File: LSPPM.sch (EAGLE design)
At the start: 340 parts, among them IC1 ATMEGA328P QFN32, IC10 ATMEGA328P QFN32, IC11 ATMEGA328P QFN32, IC12 ATMEGA328P QFN32, IC13 ATMEGA328P QFN32, IC14 ATMEGA328P QFN32, IC15 ATMEGA328P QFN32, IC16 ATMEGA328P QFN32, IC17 TXB0104, IC18 TMP102, IC19 TMP102, IC2 ATMEGA328P QFN32, IC20 ATMEGA2561-16MU, IC21 MAX4372F, IC22 MAX4372F, IC23 MUX-74HC4067-QFNSMT, IC24 MUX-74HC4067-QFNSMT, IC25 TCA9555QFN, IC3 ATMEGA328P QFN32, IC4 ATMEGA328P QFN32, IC5 ATMEGA328P QFN32, IC6 ATMEGA328P QFN32, IC7 ATMEGA328P QFN32, IC8 ATMEGA328P QFN32, IC9 ATMEGA328P QFN32, P1 microSD, Q1 RJU003N03 N-MOSFET, Q10 RJU003N03 N-MOSFET, Q11 RJU003N03 N-MOSFET, Q12 RJU003N03 N-MOSFET, Q13 RJU003N03 N-MOSFET, Q14 RJU003N03 N-MOSFET, Q15 RJU003N03 N-MOSFET, Q16 RJU003N03 N-MOSFET, Q17 RJU003N03 N-MOSFET, Q18 RJU003N03 N-MOSFET, Q19 RJU003N03 N-MOSFET, Q2 RJU003N03 N-MOSFET, Q20 RJU003N03 N-MOSFET, Q21 RJU003N03 N-MOSFET, Q22 RJU003N03 N-MOSFET, Q23 RJU003N03 N-MOSFET, Q24 RJU003N03 N-MOSFET, Q25 RJU003N03 N-MOSFET, Q26 RJU003N03 N-MOSFET, Q27 RJU003N03 N-MOSFET, Q28 RJU003N03 N-MOSFET, Q29 RJU003N03 N-MOSFET, Q3 RJU003N03 N-MOSFET, Q30 RJU003N03 N-MOSFET, Q31 RJU003N03 N-MOSFET, Q32 RJU003N03 N-MOSFET, Q33 RJU003N03 N-MOSFET, Q34 RJU003N03 N-MOSFET, Q35 RJU003N03 N-MOSFET, Q36 RJU003N03 N-MOSFET, Q37 RJU003N03 N-MOSFET, Q38 RJU003N03 N-MOSFET, Q39 RJU003N03 N-MOSFET, Q4 RJU003N03 N-MOSFET, Q40 RJU003N03 N-MOSFET, Q41 RJU003N03 N-MOSFET, Q42 RJU003N03 N-MOSFET, Q43 RJU003N03 N-MOSFET, Q44 RJU003N03 N-MOSFET, Q45 RJU003N03 N-MOSFET, Q46 RJU003N03 N-MOSFET, Q5 RJU003N03 N-MOSFET, Q6 RJU003N03 N-MOSFET, Q7 RJU003N03 N-MOSFET, Q8 RJU003N03 N-MOSFET, Q9 RJU003N03 N-MOSFET, SW1 ADG801 SOT23-6, SW10 ADG801 SOT23-6, SW11 ADG801 SOT23-6, SW12 ADG801 SOT23-6, SW13 ADG801 SOT23-6, SW14 ADG801 SOT23-6, SW15 ADG801 SOT23-6, SW16 ADG801 SOT23-6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

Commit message: Updated README and board files for public release
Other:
- note added: "(c) Copyright 2015 Freetronics Pty Ltd"
- note added: "LibreSat Payload Processor Module"
- note added: "SKU: LSPPM"
- note added: "V1.5 (2015-09-21)"
- note added: "www.libresat.org/lsppm"
- note removed: "(c) Copyright 2013 Freetronics Pty Ltd"
- note removed: "ArduSat Payload Processor Module"
- note removed: "SKU: ASPPM"
- note removed: "V1.2 (2013-02-21)"
- note removed: "www.freetronics.com/asppm"
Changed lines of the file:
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@@
 <?xml version="1.0" encoding="utf-8"?>
 <!DOCTYPE eagle SYSTEM "eagle.dtd">
-<eagle version="6.3">
+<eagle version="6.5.0">
 <drawing>
 <settings>
@@
 <sheet>
 <plain>
-<text x="149.86" y="12.7" size="3.048" layer="94">ArduSat Payload Processor Module</text>
-<text x="215.9" y="6.858" size="1.778" layer="94">V1.2 (2013-02-21)</text>
-<text x="149.606" y="6.858" size="1.778" layer="94">www.freetronics.com/asppm</text>
-<text x="190.5" y="6.858" size="1.778" layer="94">SKU: ASPPM</text>
+<text x="149.86" y="12.7" size="3.048" layer="94">LibreSat Payload Processor Module</text>
+<text x="215.9" y="6.858" size="1.778" layer="94">V1.5 (2015-09-21)</text>
+<text x="149.606" y="6.858" size="1.778" layer="94">www.libresat.org/lsppm</text>
+<text x="190.5" y="6.858" size="1.778" layer="94">SKU: LSPPM</text>
 <frame x1="0" y1="0" x2="248.92" y2="185.42" columns="8" rows="5" layer="94"/>
 <frame x1="147.32" y1="5.08" x2="243.84" y2="17.78" columns="0" rows="0" layer="94" border-left="no" border-top="no" border-right="no" border-bottom="no"/>
@@
 <text x="86.36" y="7.62" size="1.778" layer="94">Open Hardware License</text>
 <text x="86.36" y="5.08" size="1.778" layer="94">www.tapr.org/OHL</text>
-<text x="86.36" y="15.24" size="1.778" layer="94">(c) Copyright 2013 Freetronics Pty Ltd</text>
+<text x="86.36" y="15.24" size="1.778" layer="94">(c) Copyright 2015 Freetronics Pty Ltd</text>
 <wire x1="213.36" y1="68.58" x2="157.48" y2="68.58" width="0.1524" layer="97" style="longdash"/>
 <wire x1="157.48" y1="68.58" x2="73.66" y2="68.58" width="0.1524" layer="97" style="longdash"/>
@@
 <junction x="101.6" y="167.64"/>
 <junction x="104.14" y="167.64"/>
-</segment>
-</net>
+<wire x1="104.14" y1="154.94" x2="76.2" y2="154.94" width="0.1524" layer="91"/>
+<junction x="104.14" y="154.94"/>
+<label x="76.2" y="154.94" size="1.778" layer="95"/>
+</segment>
+</net>

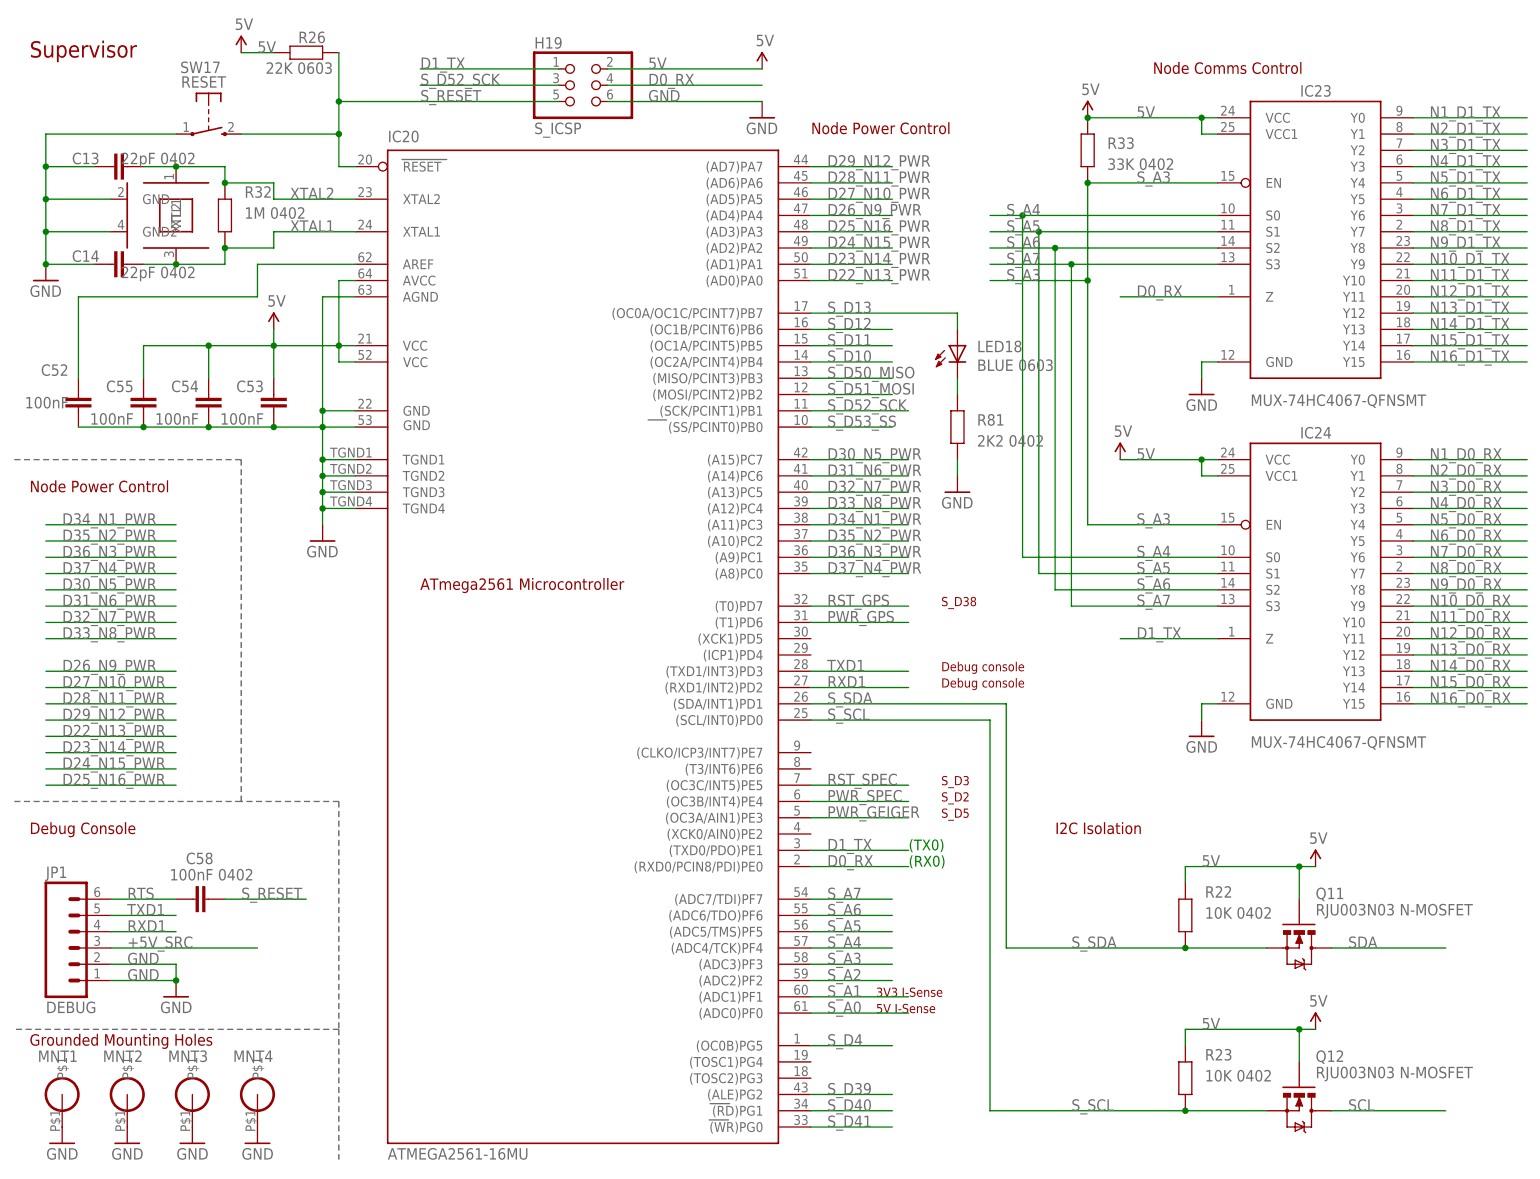
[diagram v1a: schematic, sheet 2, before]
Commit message: Replaced most parts using SuperHouse library to add 3D models
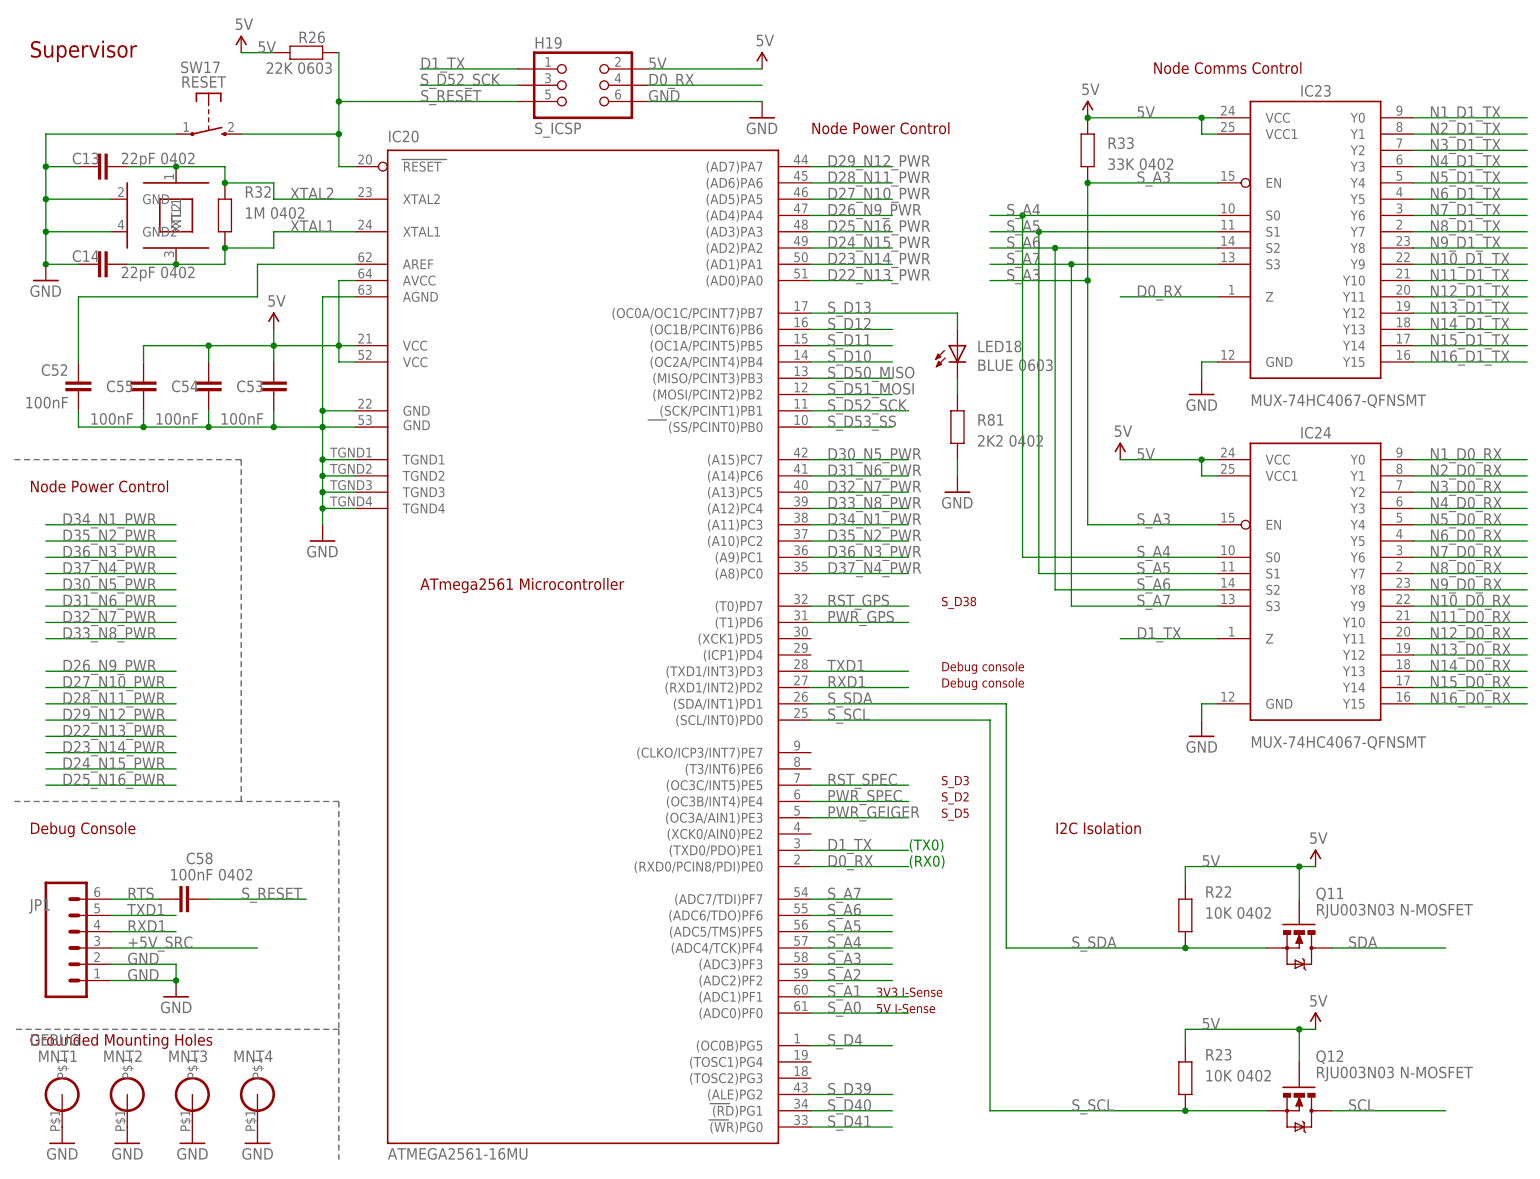
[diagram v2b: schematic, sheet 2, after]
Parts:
- C1, C12, C17, C20, C23, C26, C29, C32, C35, C38, C43, C46, C49, C57, C6, C9: device freetronics-jon:C-EUC0603 -> SuperHouse-DiscreteSemi:CAP0603
- C10, C11, C13, C14, C15, C16, C18, C19, C2, C21, C22, C24, C25, C27, C28, C3, C30, C31, C33, C34, C36, C37, C39, C4, C40, C41, C42, C44, C45, C47, C48, C5, C50, C51, C52, C53, C54, C55, C56, C58, C61, C62, C7, C8: device freetronics-jon:C-EU0402C -> SuperHouse-DiscreteSemi:CAP0402
- C59, C60: device freetronics-jon:CAP_POL1206 -> SuperHouse-DiscreteSemi:CAP_POL1206
- H1, H2: value CUBESATBUSH -> CUBESATBUS-ST; device freetronics-jon:CUBESATBUSH -> SuperHouse-Connectors:CUBESATBUS-ST
- H19: device freetronics-jon:ICSPPTH -> SuperHouse-Connectors:ICSP-PIN
- IC1, IC10, IC11, IC12, IC13, IC14, IC15, IC16, IC2, IC3, IC4, IC5, IC6, IC7, IC8, IC9: device freetronics-jon:AVR-MEGA8-MI -> SuperHouse-MCUs:ATMEGA8-MLF
- IC18, IC19: device freetronics-jon:TMP102 -> SuperHouse-Sensors:TMP102
- JP1: device freetronics-master-v1:M06RA -> SuperHouse-Connectors:M06-PIN-RIGHTANGLE
- LED17, LED18: device freetronics-jon:LED0402 -> SuperHouse-LEDs:LED0402
- P1: device freetronics-master-v1.1:USD-SOCKETNEW -> SuperHouse-Connectors:USD-SOCKETNEW
- Q1, Q10, Q11, Q12, Q13, Q14, Q15, Q16, Q17, Q18, Q19, Q2, Q20, Q21, Q22, Q23, Q24, Q25, Q26, Q27, Q28, Q29, Q3, Q30, Q31, Q32, Q33, Q34, Q35, Q36, Q37, Q38, Q39, Q4, Q40, Q41, Q42, Q43, Q44, Q45, Q46, Q5, Q6, Q7, Q8, Q9: device freetronics-jon:MOSFET-NSOT-323 -> SuperHouse-DiscreteSemi:MOSFET-NCHANNEL-323
- R1, R10, R11, R12, R13, R14, R15, R16, R17, R18, R19, R2, R20, R21, R22, R23, R24, R25, R26, R27, R28, R29, R3, R30, R31, R32, R33, R34, R35, R36, R37, R38, R39, R4, R40, R41, R42, R43, R44, R45, R46, R47, R48, R49, R5, R50, R51, R52, R53, R54, R55, R56, R57, R58, R6, R60, R61, R62, R63, R64, R65, R66, R67, R68, R69, R7, R70, R71, R72, R73, R74, R76, R77, R78, R79, R8, R80, R81, R82, R83, R84, R85, R86, R87, R88, R89, R9, R90: device freetronics-jon:RESISTOR0402 -> SuperHouse-DiscreteSemi:RESISTOR0402
- R59, R75: device freetronics-original:RESISTOR2010 -> SuperHouse-DiscreteSemi:RESISTOR2010
- RN1, RN10, RN11, RN12, RN13, RN14, RN15, RN16, RN2, RN3, RN4, RN5, RN6, RN7, RN8, RN9: device resistor-dil:4R-NCAY16 -> SuperHouse-DiscreteSemi:4R-NCAY16
- RN17, RN18: device freetronics-master-v1:4R-NCAY16 -> SuperHouse-DiscreteSemi:4R-NCAY16
- SW17: device freetronics-master-v1:TAC_SWITCH_2PIN -> SuperHouse-Switches:TAC_SWITCH_2PINSMT
- X1: device con-molex:53398-06 -> SuperHouse-Connectors:PICOBLADE-53398-06
- X2: device con-molex:53398-08 -> SuperHouse-Connectors:PICOBLADE-53398-08
- X3: device con-molex:53398-07 -> SuperHouse-Connectors:PICOBLADE-53398-07
- XTL1, XTL10, XTL11, XTL12, XTL13, XTL14, XTL15, XTL16, XTL17, XTL2, XTL3, XTL4, XTL5, XTL6, XTL7, XTL8, XTL9: device freetronics-jon:CRYSTAL-GND3X2 -> SuperHouse-Oscillators:CRYSTAL-GND3X2
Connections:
- net GND: no longer IC1.TGND, IC10.TGND, IC11.TGND, IC12.TGND, IC13.TGND, IC14.TGND, IC15.TGND, IC16.TGND, IC2.TGND, IC3.TGND, IC4.TGND, IC5.TGND, IC6.TGND, IC7.TGND, IC8.TGND, IC9.TGND
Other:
- moved on the sheet: C10, C11, C13, C14, C15, C16, C18, C19, C2, C21, C22, C24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
